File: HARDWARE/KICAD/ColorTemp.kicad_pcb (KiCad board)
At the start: 2 copper layers, 2 parts, among them U1 CH32V003F4U6

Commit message: Advancing on parts creation.
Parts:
- added R1: 1K 1%, ColorTemp:R_0603_1608Metric, F.Cu at (161.7, 89.0)
- added R2: 1K 1%, ColorTemp:R_0603_1608Metric, F.Cu at (161.7, 91.5)
- added R3: 1K 1%, ColorTemp:R_0603_1608Metric, F.Cu at (161.7, 94.0)

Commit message: Added most of the components. Recently project started crashing on PCB, when I press X to route. I'll try to restore a backup.
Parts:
- added C2: 10uF 25V, ColorTemp:C_0805_2012Metric, F.Cu at (146.0, 100.0)
- added C3: 10uF 25V, ColorTemp:C_0805_2012Metric, F.Cu at (144.5, 90.0)
- added C4: 100nF 50V, ColorTemp:C_0402_1005Metric, F.Cu at (158.2, 98.8)
- added D1: RGB, ColorTemp:LED_RGB_5050-6, F.Cu at (150.0, 100.0)
- added G***: LOGO, LOGO, B.Cu at (157.5, 97.8)
- added H1: MountingHole, ColorTemp:MountingHole_3.2mm_M3, F.Cu at (138.8, 88.8)
- added H2: MountingHole, ColorTemp:MountingHole_3.2mm_M3, F.Cu at (161.2, 88.8)
- added H3: MountingHole, ColorTemp:MountingHole_3.2mm_M3, F.Cu at (138.8, 111.2)
- added H4: MountingHole, ColorTemp:MountingHole_3.2mm_M3, F.Cu at (161.2, 111.2)
- added J1: Conn_02x05_Odd_Even, ColorTemp:PinHeader_2x05_P2.54mm_Vertical, B.Cu at (144.9, 109.7)
- added J2: USB_C_Receptacle_PowerOnly_6P, ColorTemp:USB_C_Receptacle_GCT_USB4125-xx-x-0190_6P_TopMnt_Horizontal, F.Cu at (138.5, 100.0)
- added Q1: MMBT3904, ColorTemp:SOT-23, F.Cu at (146.5, 93.8)
- added Q2: MMBT3904, ColorTemp:SOT-23, F.Cu at (150.0, 93.8)
- added Q3: MMBT3904, ColorTemp:SOT-23, F.Cu at (153.5, 93.8)
- added R4: 1K 1%, ColorTemp:R_0402_1005Metric, F.Cu at (157.0, 93.5)
- added R5: 1K 1%, ColorTemp:R_0402_1005Metric, F.Cu at (162.8, 94.0)
- added R6: 1K 1%, ColorTemp:R_0402_1005Metric, F.Cu at (159.2, 98.8)
- added R7: 5.1K 1%, ColorTemp:R_0402_1005Metric, F.Cu at (144.0, 100.5)
- added R8: 5.1K 1%, ColorTemp:R_0402_1005Metric, F.Cu at (144.0, 99.5)
- added R9: 5.1K 1%, ColorTemp:R_0402_1005Metric, F.Cu at (157.2, 98.8)
- added U2: MCP9700A, ColorTemp:SOT-23, F.Cu at (160.0, 105.0)
- moved C1 16.9 mm to (162.8, 96.0)
- moved R1 15.2 mm to (146.5, 90.0), turned to -90 degrees
- moved R2 11.8 mm to (150.0, 90.0), turned to -90 degrees
- moved U1 10.8 mm to (160.0, 95.0), turned to 90 degrees
- moved R3 9.10 mm to (153.5, 90.0), turned to -90 degrees
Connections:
- R1 pad 2: unconnected-(R1-Pad2) -> /Q B
- R2 pad 2: unconnected-(R2-Pad2) -> /Q R
- R3 pad 2: unconnected-(R3-Pad2) -> /Q G
- U1 pad 1: unconnected-(U1-PD7-Pad1) -> ~{RESET}
- U1 pad 10: unconnected-(U1-PC3-Pad10) -> /MCU PC3
- U1 pad 16: unconnected-(U1-PD2-Pad16) -> /MCU PD2
- U1 pad 2: unconnected-(U1-PA1-Pad2) -> /MCU PA1
- U1 pad 3: unconnected-(U1-PA2-Pad3) -> TEMPERATURE
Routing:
- net +5V: track 0.00 -> 66.6 mm
- net GND: track 0.00 -> 28.0 mm
- net LED BLUE: track 0.00 -> 18.2 mm
- net LED RED: track 0.00 -> 12.4 mm
- net TEMPERATURE: track 0.00 -> 8.01 mm
- net /LED G: track 0.00 -> 5.37 mm
- net /LED R: track 0.00 -> 3.31 mm
- net /LED B: track 0.00 -> 3.26 mm
- net ~{RESET}: track 0.00 -> 3.23 mm
- net LED GREEN: track 0.00 -> 2.69 mm
- net /MCU PA1: track 0.00 -> 1.93 mm
- net Net-(J2-CC2): track 0.00 -> 1.91 mm
- net Net-(J2-CC1): track 0.00 -> 1.91 mm
- net /MCU PC3: track 0.00 -> 1.43 mm
- added copper zone on B.Cu, net GND
- added copper zone on F.Cu, net GND
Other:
- board outline added: 30 x 30 mm
- board text added: "(symbol "LOGO" (pin_names (offset 1.016)) (in_bom yes) (on_board yes) (property "Reference" "#G" (at 0 4.5648 0) (effects (font (size 1.27 1.27)) hide) ) (property "Value" "LOGO" (at 0 -4.5648 0) (effects (font (size 1.27 1.27)) hide) ) (property "Footprint" "" (at 0 0 0) (effects (font (size 1.27 1.27)) hide) ) (property "Datasheet" "" (at 0 0 0) (effects (font (size 1.27 1.27)) hide) ) (symbol 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"
- board text added: "MechatronixLab ColorTemp Rev.00 2026.03.08"

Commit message: Restored working project.
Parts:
- removed G***: LOGO, LOGO
- J1: moved to F.Cu
- moved J1 2.55 mm to (144.9, 112.3), turned to 90 degrees
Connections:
- J1 pad 1: +5V -> GND
- J1 pad 2: GND -> +5V
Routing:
- net +5V: track 66.6 -> 73.6 mm
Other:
- board text removed: "(symbol "LOGO" (pin_names (offset 1.016)) (in_bom yes) (on_board yes) (property "Reference" "#G" (at 0 4.5648 0) (effects (font (size 1.27 1.27)) hide) ) (property "Value" "LOGO" (at 0 -4.5648 0) (effects (font (size 1.27 1.27)) hide) ) (property "Footprint" "" (at 0 0 0) (effects (font (size 1.27 1.27)) hide) ) (property "Datasheet" "" (at 0 0 0) (effects (font (size 1.27 1.27)) hide) ) (symbol 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"
- board text removed: "MechatronixLab ColorTemp Rev.00 2026.03.08"

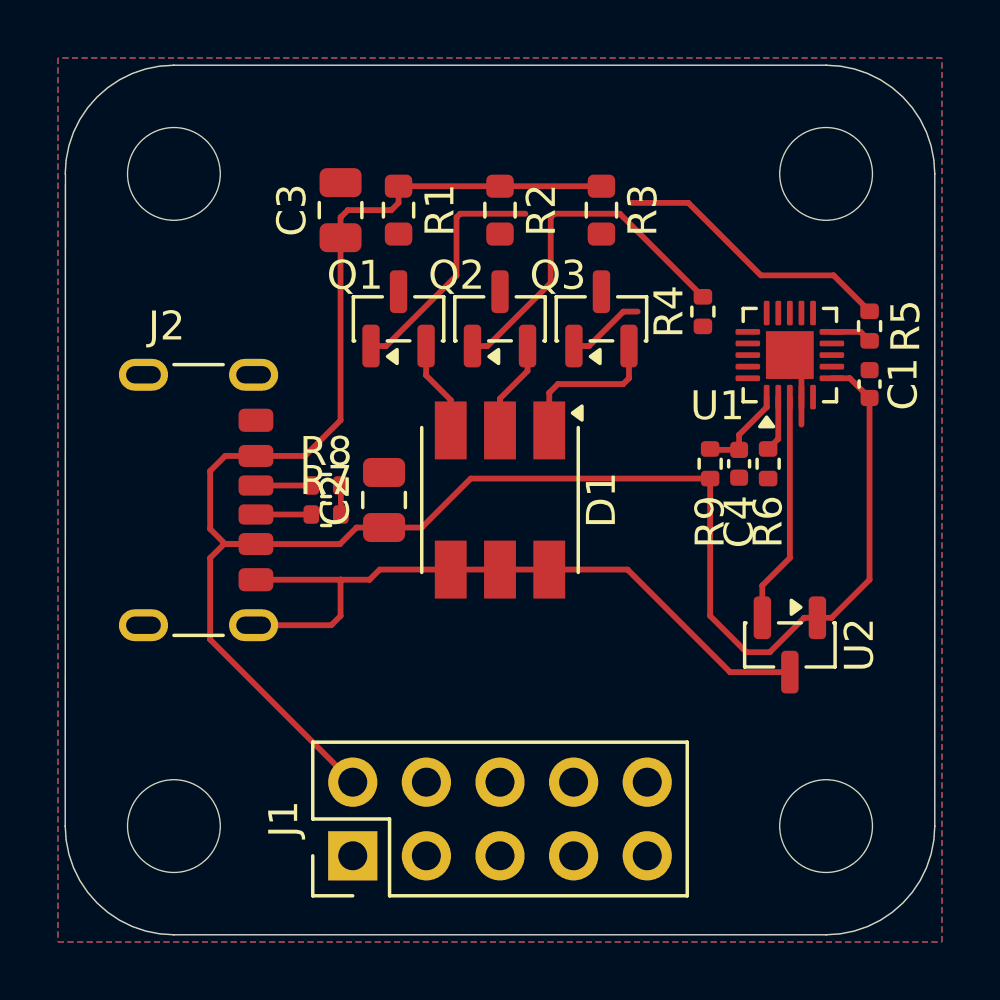
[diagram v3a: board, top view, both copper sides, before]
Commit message: Project restored and back to normal. Added signals to external connector.
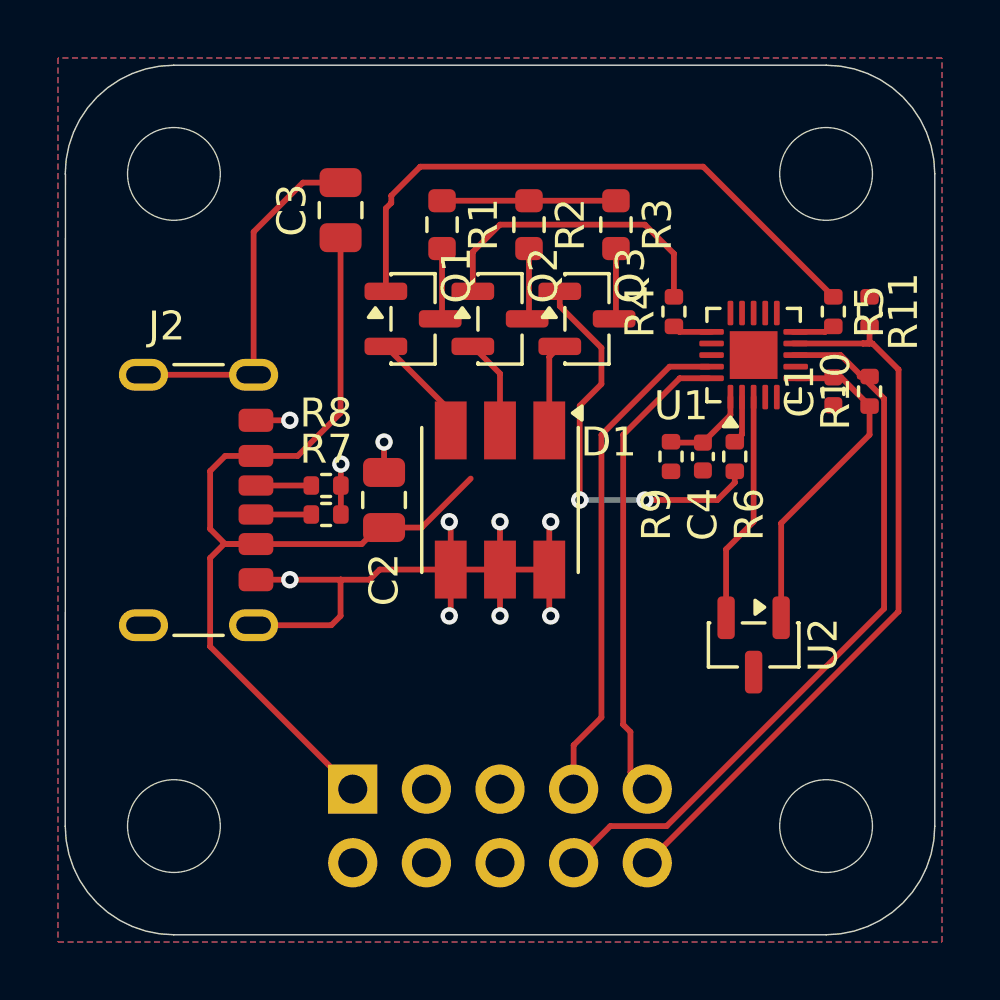
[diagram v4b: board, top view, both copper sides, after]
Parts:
- added R10: 5.1K 1%, ColorTemp:R_0402_1005Metric, F.Cu at (162.8, 96.2)
- added R11: 5.1K 1%, ColorTemp:R_0402_1005Metric, F.Cu at (162.8, 93.5)
- J1: moved to B.Cu
- moved J1 2.30 mm to (144.9, 110.0), turned to -90 degrees
- moved R1 1.58 mm to (148.0, 90.5)
- moved R9 1.37 mm to (155.9, 98.5)
- moved R5 1.35 mm to (161.5, 93.5)
- moved C1 1.27 mm to (161.5, 96.2), turned to 90 degrees
- moved C4 1.27 mm to (157.0, 98.5)
- moved U1 1.25 mm to (158.8, 95.0)
- moved U2 1.25 mm to (158.8, 105.0)
- moved R6 1.18 mm to (158.1, 98.5)
- moved R2 1.12 mm to (151.0, 90.5)
- moved R4 1.00 mm to (156.0, 93.5)
- moved R3 0.71 mm to (154.0, 90.5)
- moved Q1 0.50 mm to (147.0, 93.8), turned to 0 degrees
- moved Q3 0.50 mm to (153.0, 93.8), turned to 0 degrees
- turned Q2 to 0 degrees
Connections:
- J1 pad 1: GND -> +5V
- J1 pad 10: unconnected-(J1-Pin_10-Pad10) -> I2C SCL
- J1 pad 2: +5V -> GND
- J1 pad 7: unconnected-(J1-Pin_7-Pad7) -> UART TX
- J1 pad 8: unconnected-(J1-Pin_8-Pad8) -> I2C SDA
- J1 pad 9: unconnected-(J1-Pin_9-Pad9) -> UART RX
- U1 pad 19: unconnected-(U1-PD5-Pad19) -> UART TX
- U1 pad 20: unconnected-(U1-PD6-Pad20) -> UART RX
- U1 pad 8: unconnected-(U1-PC1-Pad8) -> I2C SDA
- U1 pad 9: unconnected-(U1-PC2-Pad9) -> I2C SCL
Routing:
- net I2C SCL: track 0.00 -> 25.4 mm
- net I2C SDA: track 0.00 -> 25.4 mm
- net +5V: track 73.6 -> 52.9 mm
- net UART TX: track 0.00 -> 17.3 mm
- net UART RX: track 0.00 -> 16.3 mm
- net GND: track 28.0 -> 40.9 mm, vias 0 -> 10
- net LED GREEN: track 2.69 -> 14.1 mm, vias 0 -> 2
- net LED BLUE: track 18.2 -> 20.9 mm
- net /Q R: track 0.00 -> 2.45 mm
- net /Q G: track 0.00 -> 2.45 mm
- net /Q B: track 0.00 -> 2.45 mm
- net /LED G: track 5.37 -> 3.05 mm
- net LED RED: track 12.4 -> 10.6 mm
- net /MCU PD2: track 0.00 -> 1.38 mm
- net /LED B: track 3.26 -> 3.83 mm

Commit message: Removed transistors for driving LED. Advanced circuit and layout design. Added switches.
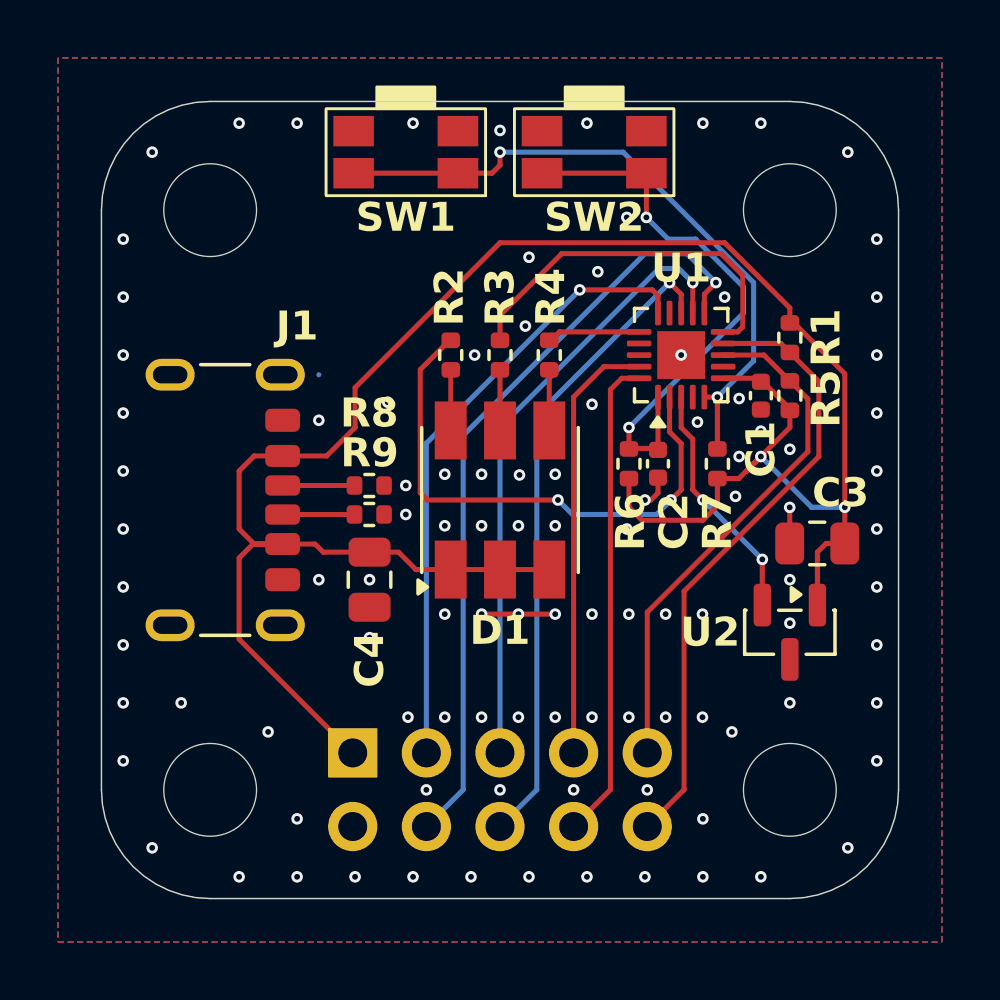
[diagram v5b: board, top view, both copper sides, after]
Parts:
- removed Q1, Q2, Q3: MMBT3904, ColorTemp:SOT-23
- removed the R1 at (148.0, 90.5)
- removed the R2 at (151.0, 90.5)
- removed the R3 at (154.0, 90.5)
- added R7: 5.1K 1%, ColorTemp:R_0402_1005Metric, F.Cu at (157.5, 98.8)
- added SW1: SW_Push, ColorTemp:EVQP7A01P, F.Cu at (146.8, 88.0)
- added SW2: ~{RESET}, ColorTemp:EVQP7A01P, F.Cu at (153.2, 88.0)
- moved C3 20.1 mm to (160.9, 101.5), turned to 0 degrees
- moved R3 11.6 mm to (150.0, 95.0), turned to -90 degrees
- moved R2 10.4 mm to (148.3, 95.0)
- moved R4 4.55 mm to (151.7, 95.0), turned to -90 degrees
- moved R1 2.89 mm to (160.0, 94.4)
- moved C4 2.80 mm to (145.5, 102.8), turned to -90 degrees
- moved R5 2.75 mm to (160.0, 96.4)
- moved C1 2.50 mm to (159.0, 96.4)
- moved U1 2.50 mm to (156.2, 95.0)
- moved H1 1.77 mm to (140.0, 90.0)
- moved H2 1.77 mm to (160.0, 90.0)
- moved H3 1.77 mm to (140.0, 110.0)
- moved H4 1.77 mm to (160.0, 110.0)
- moved C2 1.57 mm to (155.4, 98.8)
- moved R8 1.49 mm to (145.5, 99.5)
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- renumbered C4 to C2, C2 to C4, J2 to J1, J1 to J2, R11 to R1, R6 to R2, R5 to R3, R10 to R5, R9 to R6, R7 to R9
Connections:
- C3 pad 1: +5V -> GND
- C3 pad 2: GND -> +5V
- D1 pad 1: /LED G -> +5V
- D1 pad 2: /LED R -> +5V
- D1 pad 3: /LED B -> +5V
- D1 pad 4: GND -> LED BLUE
- D1 pad 5: GND -> LED RED
- D1 pad 6: GND -> LED GREEN
- J2 pad 3: unconnected-(J1-Pin_3-Pad3) -> DIO
- J2 pad 4: unconnected-(J1-Pin_4-Pad4) -> PC4
- J2 pad 5: unconnected-(J1-Pin_5-Pad5) -> PC5
- J2 pad 6: unconnected-(J1-Pin_6-Pad6) -> PC6
- J2 pad 8: I2C SDA -> UART RX
- J2 pad 9: UART RX -> I2C SDA
- R3 pad 2: LED BLUE -> LED RED
- R4 pad 2: LED RED -> LED BLUE
- U1 pad 11: unconnected-(U1-PC4-Pad11) -> PC4
- U1 pad 12: unconnected-(U1-PC5-Pad12) -> PC5
- U1 pad 13: unconnected-(U1-PC6-Pad13) -> PC6
- U1 pad 5: unconnected-(U1-PD0-Pad5) -> USER
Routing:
- net GND: track 40.9 -> 5.88 mm, vias 10 -> 102
- net PC4: track 0.00 -> 27.0 mm, vias 0 -> 1
- net +5V: track 52.9 -> 75.8 mm, vias 0 -> 2
- net USER: track 0.00 -> 22.9 mm, vias 0 -> 2
- net PC6: track 0.00 -> 22.4 mm, vias 0 -> 1
- net DIO: track 0.00 -> 21.5 mm, vias 0 -> 1
- net PC5: track 0.00 -> 21.4 mm, vias 0 -> 1
- net LED BLUE: track 20.9 -> 2.09 mm
- net /MCU PA1: track 1.64 -> 18.7 mm, vias 0 -> 2
- net ~{RESET}: track 3.08 -> 19.5 mm, vias 0 -> 2
- net LED GREEN: track 14.1 -> 2.09 mm, vias 2 -> 0
- net /MCU PC3: track 1.38 -> 13.0 mm
- net LED RED: track 10.6 -> 2.09 mm
- net I2C SDA: track 25.4 -> 18.1 mm
- net /LED B: track 3.83 -> 0.00 mm
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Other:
- board size 30 x 30 mm -> 27.5 x 27.5 mm

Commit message: Detailing layout and silkscreen.
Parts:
- added G***: LOGO, LOGO, B.Cu at (150.0, 96.0)
- J1: value USB_C_Receptacle_PowerOnly_6P -> POWER
- SW1: value SW_Push -> USER
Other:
- board text added: "5V G"
- board text added: "C5 C6"
- board text added: "DA CL"
- board text added: "DIO C4"
- board text added: "Mechatronix Lab Rev.00 2026.03.14"
- board text added: "TX RX"

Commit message: Preliminary PCB design done. Will now begin mechanical design.
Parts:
- added G***: LOGO, LOGO, F.Cu at (156.3, 94.8)
- moved H1 20.0 mm to (160.0, 90.0), turned to -90 degrees
- moved H2 20.0 mm to (160.0, 110.0), turned to -90 degrees
- moved H3 20.0 mm to (140.0, 90.0), turned to -90 degrees
- moved H4 20.0 mm to (140.0, 110.0), turned to -90 degrees
- moved SW1 17.6 mm to (162.0, 96.8), turned to 90 degrees
- moved SW2 17.6 mm to (162.0, 103.2), turned to 90 degrees
- moved R1 16.2 mm to (155.6, 110.0), turned to 180 degrees
- moved C3 15.6 mm to (148.5, 110.9), turned to -90 degrees
- moved U2 15.5 mm to (145.4, 110.0), turned to 180 degrees
- moved R5 15.0 mm to (153.6, 110.0), turned to 0 degrees
- moved J1 15.0 mm to (150.0, 89.4), turned to 180 degrees
- moved J2 14.3 mm to (141.3, 94.9), turned to 180 degrees
- moved C1 13.7 mm to (153.6, 109.0), turned to 0 degrees
- moved U1 11.3 mm to (155.0, 106.2), turned to 0 degrees
- moved R7 10.8 mm to (151.2, 107.5), turned to 0 degrees
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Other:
- board text added: "Color Temp R.0"
- board text added: "ColorTemp"
